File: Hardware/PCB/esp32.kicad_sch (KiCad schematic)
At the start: 6 parts, among them U1 ESP32-S3-WROOM-1

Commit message: added a lot of stuff, going to work on LCD + Touch next
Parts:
- removed R2, R3: 10k, Resistor_SMD:R_0603_1608Metric_Pad0.98x0.95mm_HandSolder, symbol Device:R_Small
- removed U1: ESP32-S3-WROOM-1, RF_Module:ESP32-S3-WROOM-1, symbol RF_Module:ESP32-S3-WROOM-1
- added C14: 1uF, Capacitor_SMD:C_0805_2012Metric_Pad1.18x1.45mm_HandSolder, symbol Device:C_Small
- added C15: 0.1uF, Capacitor_SMD:C_0603_1608Metric_Pad1.08x0.95mm_HandSolder, symbol Device:C_Small
- added D1: BAT60AE6327HTSA1, Diode_SMD:D_SOD-323_HandSoldering, symbol Device:D_Schottky
- added IC3: ESP32-WROVER-E-N8R8, Custom Footprints:ESP32WROVEREN8R8, symbol Custom Symbols:ESP32-WROVER-E-N8R8
- added J3: Programmer, Vendor_Footprints:61200621621, symbol Connector_Generic:Conn_02x03_Odd_Even
- added R2, R6: 10k, Resistor_SMD:R_0603_1608Metric_Pad0.98x0.95mm_HandSolder, symbol Device:R_US
- added SW1: ~, Vendor_Footprints:PTS647SN50SMTR2LFS, symbol Vendor_Symbols:PTS647SN50SMTR2_LFS
- C10: value 0.1u -> 10uF; footprint Capacitor_SMD:C_0603_1608Metric_Pad1.08x0.95mm_HandSolder -> Capacitor_SMD:C_0805_2012Metric; DigiKey Link (none) -> https://www.digikey.com/en/products/detail/samsung-electro-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; MPN (none) -> GRM21BR61H106KE43L; Manufacturer (none) -> Murata Electronics
- C11: value 22u -> 0.1uF; footprint Capacitor_SMD:C_0603_1608Metric_Pad1.08x0.95mm_HandSolder -> Capacitor_SMD:C_0805_2012Metric_Pad1.18x1.45mm_HandSolder; DigiKey Link (none) -> https://www.digikey.com/en/products/detail/samsung-electro-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; MPN (none) -> CL21B104KBCNFNC; Manufacturer (none) -> Samsung Electro-Mechanics
- C9: value 1u -> 10uF; footprint Capacitor_SMD:C_0603_1608Metric_Pad1.08x0.95mm_HandSolder -> Capacitor_SMD:C_0805_2012Metric; DigiKey Link (none) -> https://www.digikey.com/en/products/detail/samsung-electro-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; MPN (none) -> GRM21BR61H106KE43L; Manufacturer (none) -> Murata Electronics
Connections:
- net +3.3V: now also C10.1, C11.1, C9.1, IC3.2 (3V3), R6.1; no longer C10.2, C11.2
- net GND: now also C10.2, C11.2, C9.2, C14.2, IC3.1 (GND_1), IC3.15 (GND_2), IC3.38 (GND_3), IC3.39 (GND_4), IC3.40 (GND_5), IC3.41 (GND_6), IC3.42 (GND_7), IC3.43 (GND_8), IC3.44 (GND_9), IC3.45 (GND_10), IC3.46 (GND_11), IC3.47 (GND_12), J3.4 (Pin_4), R2.2, SW1.3; no longer C10.1, C11.1, C9.1
- new net: D1.2 (A), J3.2 (Pin_2)
- new net: C15.1, SW1.2
- new net: C15.2, SW1.4
- new net +5V: D1.1 (K)
- new net D12: IC3.14 (IO12), R2.1
- new net D13: IC3.16 (IO13)
- new net D14: IC3.13 (IO14)
- new net D15: IC3.23 (IO15)
- new net D18: IC3.30 (IO18)
- new net D19: IC3.31 (IO19)
- new net D2: IC3.24 (IO2)
- new net D21: IC3.33 (IO21)
- new net D22: IC3.36 (IO22)
- new net D23: IC3.37 (IO23)
- new net D25: IC3.10 (IO25)
- new net D26: IC3.11 (IO26)
- new net D27: IC3.12 (IO27)
- new net D32: IC3.8 (IO32)
- new net D33: IC3.9 (IO33)
- new net D34: IC3.6 (IO34)
- new net D35: IC3.7 (IO35)
- new net D36: IC3.4 (SENSOR_VP)
- new net D39: IC3.5 (SENSOR_VN)
- new net D4: IC3.26 (IO4)
- new net D5: IC3.29 (IO5)
- new net ESP-EN: C14.1, IC3.3 (EN), J3.1 (Pin_1), R6.2, SW1.1
- new net ESP-IO0: IC3.25 (IO0), J3.6 (Pin_6)
- new net ESP-RX: IC3.34 (RXD0), J3.5 (Pin_5)
- new net ESP-TX: IC3.35 (TXD0), J3.3 (Pin_3)
- no-connect marks 3 -> 9
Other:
- note added: "Espressif says that IO12 should be kept low when the module is powered on."
- note added: "For recommended soft-start"
- note added: "Recommended decoupling caps"

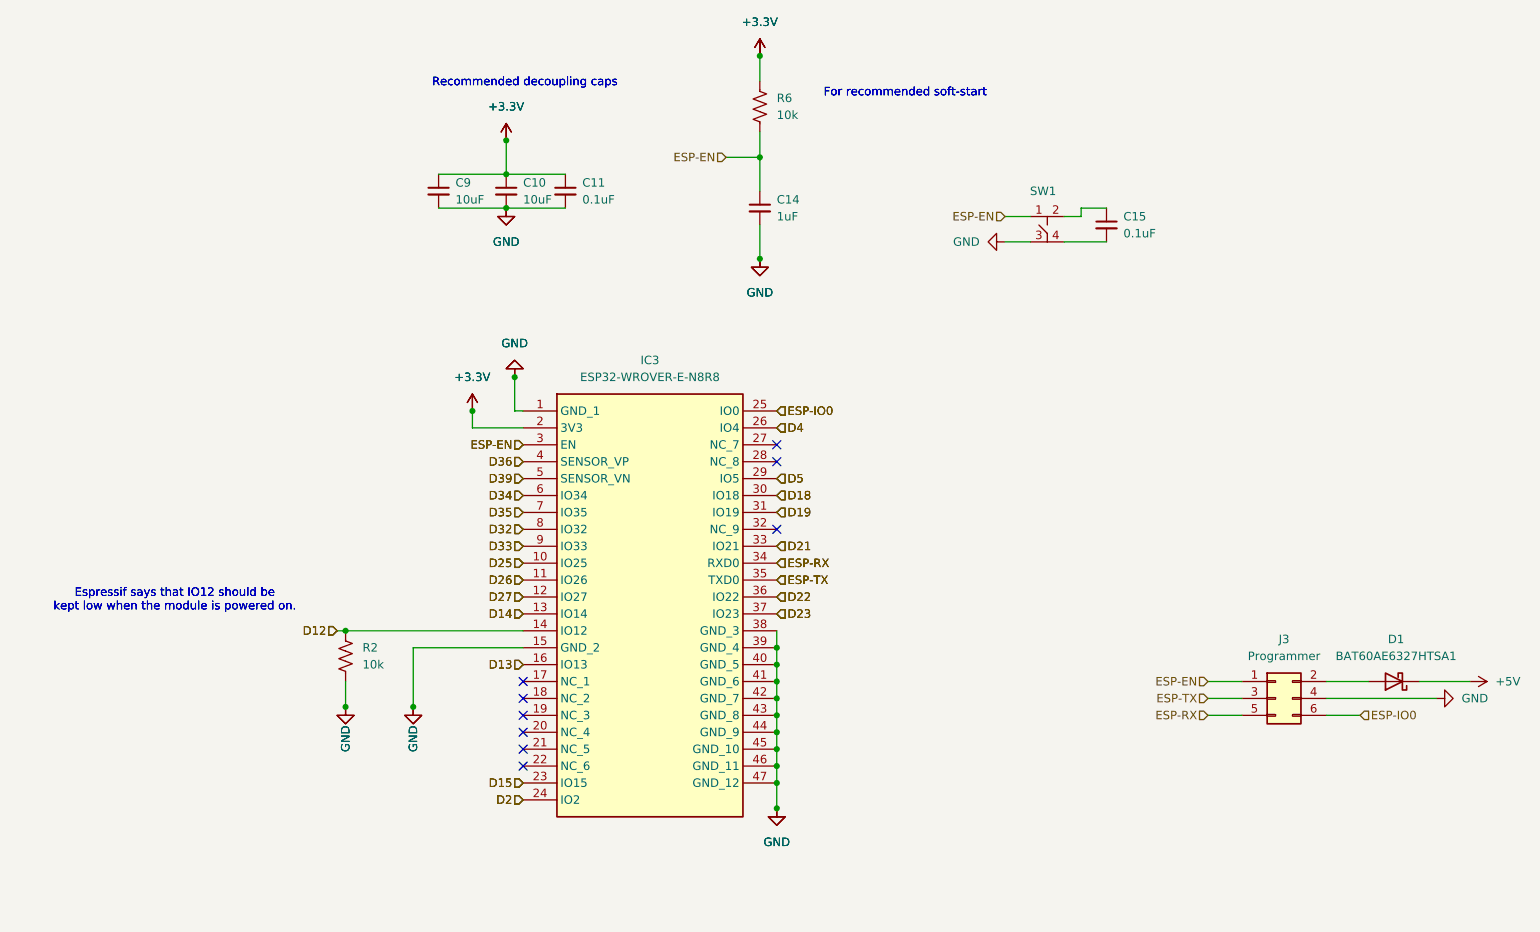
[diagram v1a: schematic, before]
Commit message: switched to making buck converter to save costs and space, and to allow for LDO after 5.5V for better stability
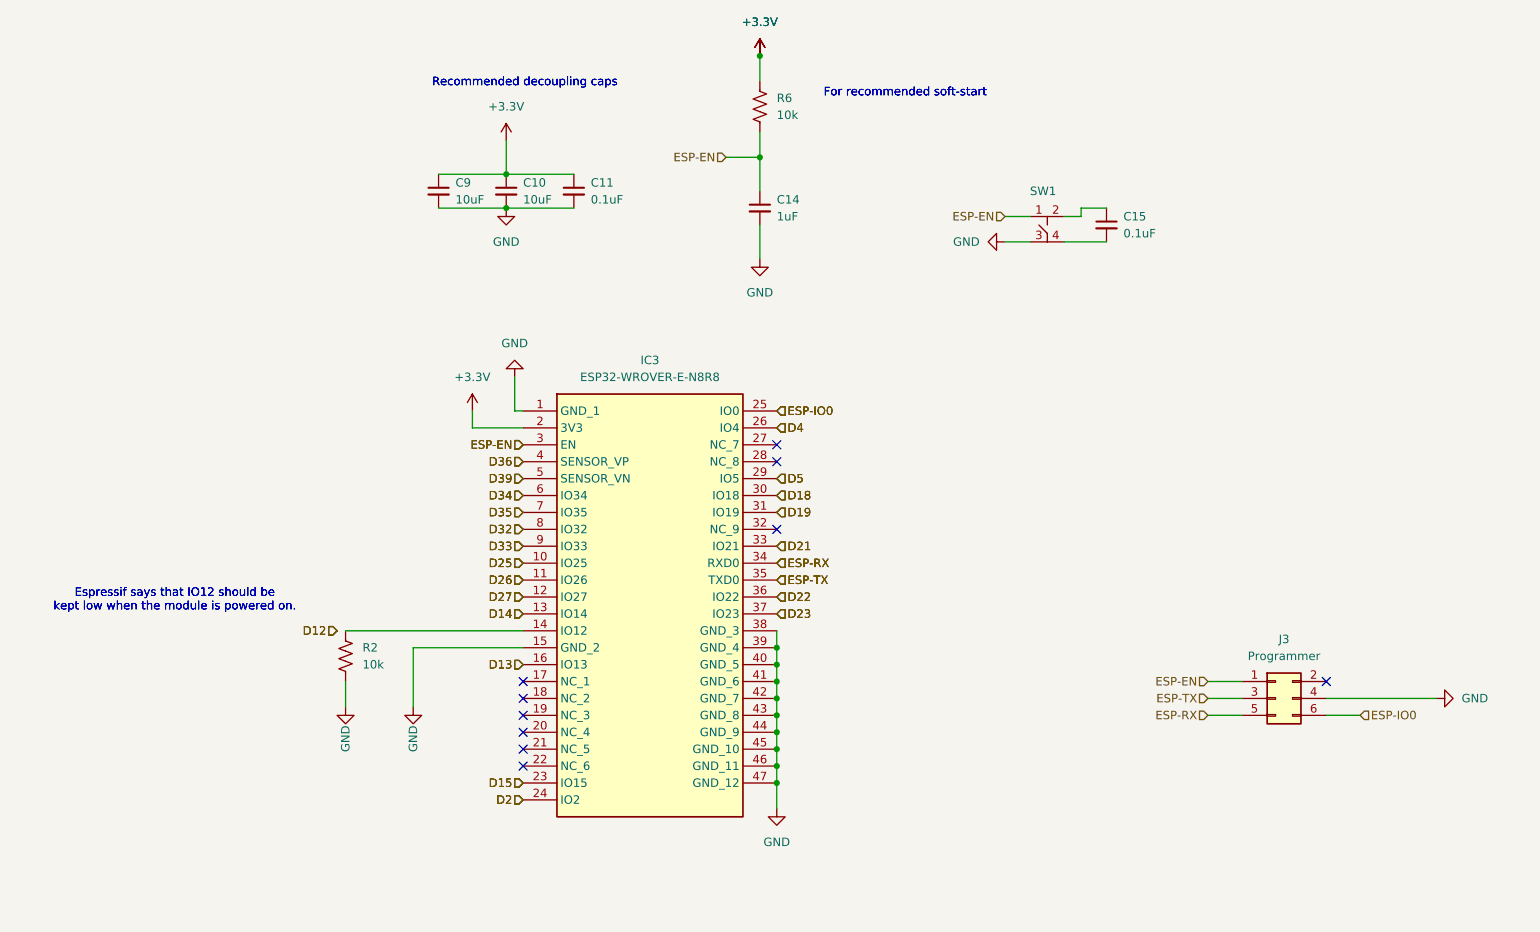
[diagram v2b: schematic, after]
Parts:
- removed D1: BAT60AE6327HTSA1, Diode_SMD:D_SOD-323_HandSoldering, symbol Device:D_Schottky
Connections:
- net D12: no longer IC3.14 (IO12), R2.1
- new net: IC3.14 (IO12), R2.1
- no-connect marks 9 -> 10
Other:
- moved on the sheet: C11

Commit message: consolidated IO for LCD block, broke out hierarchial pins, need to start wiring everything up and then on to layout
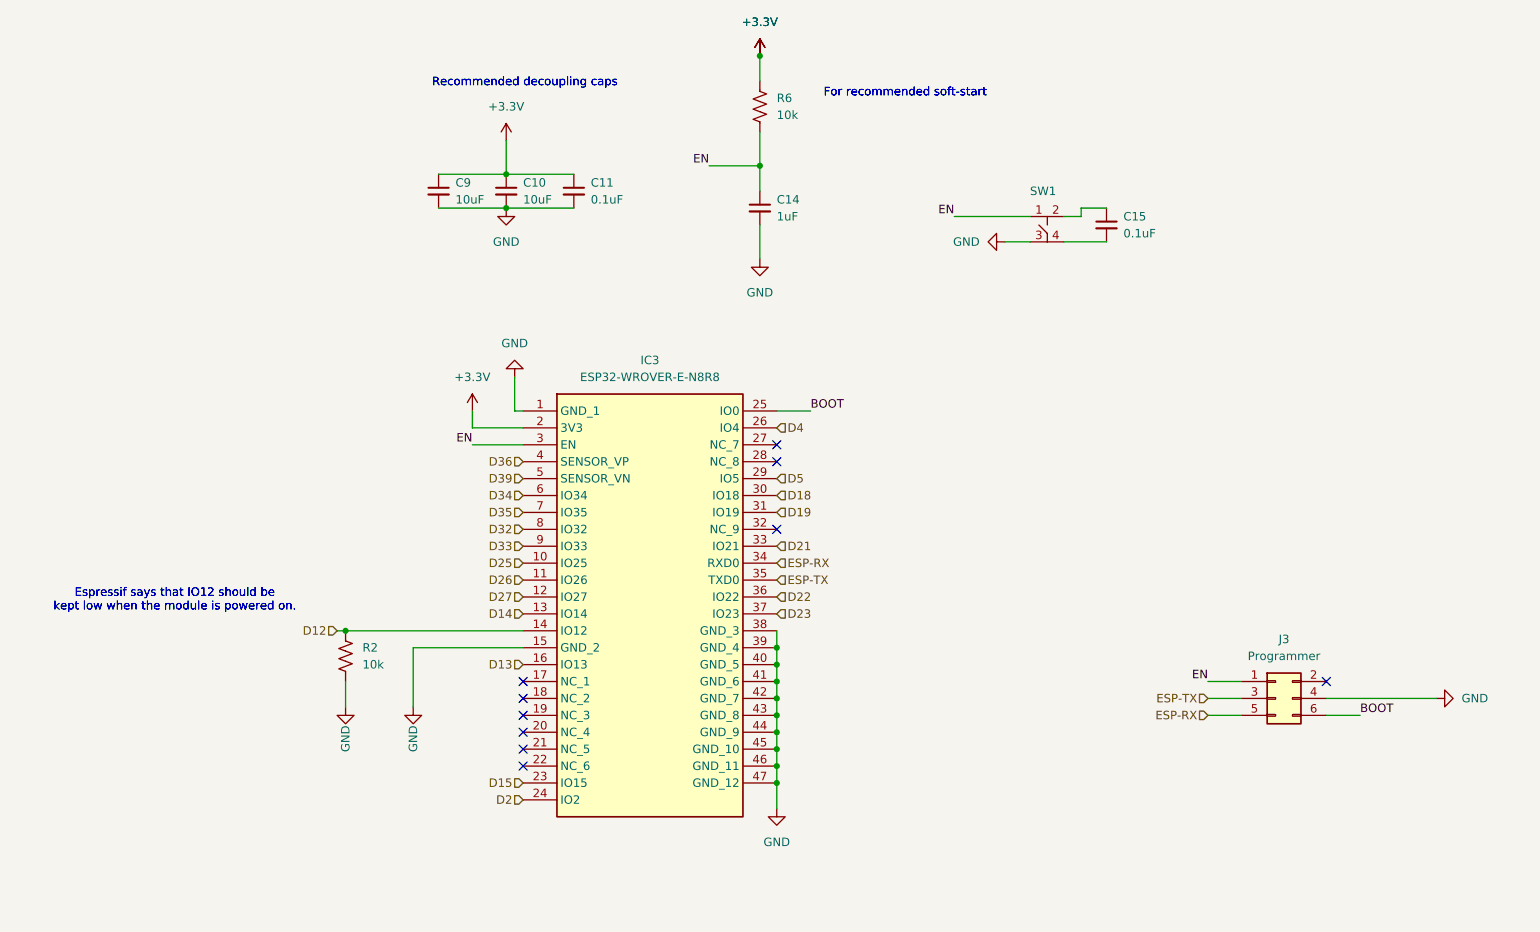
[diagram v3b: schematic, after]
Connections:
- net D12: now also IC3.14 (IO12), R2.1
- net ESP-EN renamed EN
- net ESP-IO0 renamed BOOT

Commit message: overall design is pretty much done, starting layout and routing now
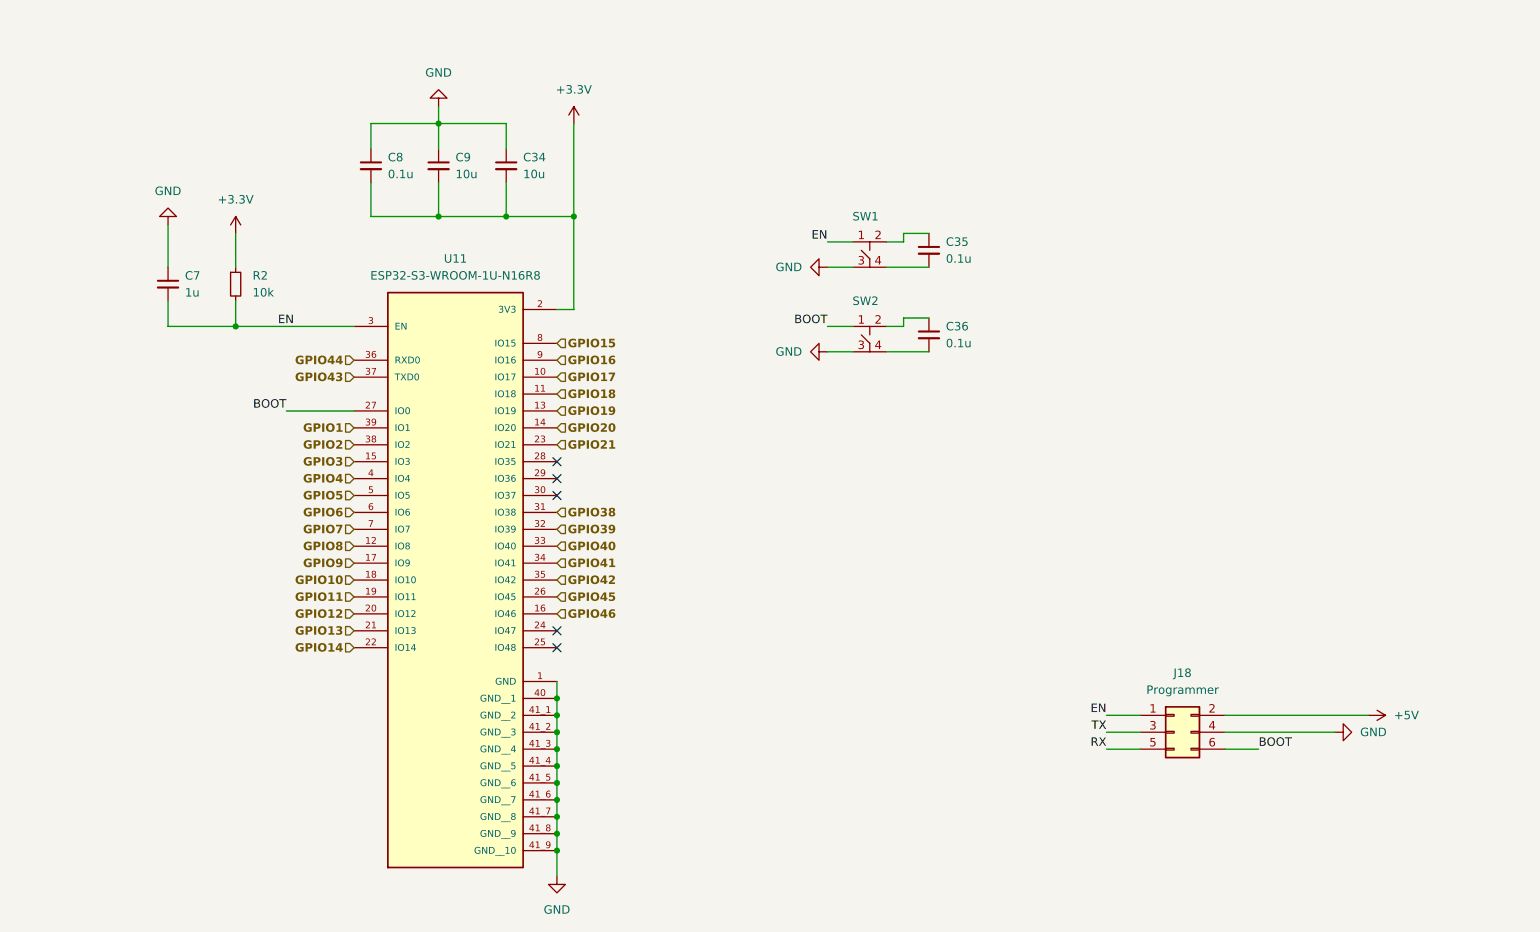
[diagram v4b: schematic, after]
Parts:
- removed C10: 10uF, Capacitor_SMD:C_0805_2012Metric, symbol Device:C_Small
- removed C11: 0.1uF, Capacitor_SMD:C_0805_2012Metric_Pad1.18x1.45mm_HandSolder, symbol Device:C_Small
- removed C14: 1uF, Capacitor_SMD:C_0805_2012Metric_Pad1.18x1.45mm_HandSolder, symbol Device:C_Small
- removed C15: 0.1uF, Capacitor_SMD:C_0603_1608Metric_Pad1.08x0.95mm_HandSolder, symbol Device:C_Small
- removed IC3: ESP32-WROVER-E-N8R8, Custom Footprints:ESP32WROVEREN8R8, symbol Custom Symbols:ESP32-WROVER-E-N8R8
- removed J3: Programmer, Vendor_Footprints:61200621621, symbol Connector_Generic:Conn_02x03_Odd_Even
- removed R2, R6: 10k, Resistor_SMD:R_0603_1608Metric_Pad0.98x0.95mm_HandSolder, symbol Device:R_US
- added C34: 10u, Capacitor_SMD:C_0805_2012Metric_Pad1.18x1.45mm_HandSolder, symbol Device:C_Small
- added C35, C36, C8: 0.1u, Capacitor_SMD:C_0603_1608Metric_Pad1.08x0.95mm_HandSolder, symbol Device:C_Small
- added C7: 1u, Capacitor_SMD:C_0603_1608Metric_Pad1.08x0.95mm_HandSolder, symbol Device:C_Small
- added J18: Programmer, Vendor_Footprints:61200621621, symbol Connector_Generic:Conn_02x03_Odd_Even
- added R2: 10k, Resistor_SMD:R_0603_1608Metric_Pad0.98x0.95mm_HandSolder, symbol Device:R_Small
- added SW2: ~, Vendor_Footprints:PTS647SN50SMTR2LFS, symbol Vendor_Symbols:PTS647SN50SMTR2_LFS
- added U11: ESP32-S3-WROOM-1U-N16R8, Vendor_Footprints:XCVR_ESP32-S3-WROOM-1U-N16R8, symbol Vendor_Symbols:ESP32-S3-WROOM-1U-N16R8
- C9: value 10uF -> 10u; footprint Capacitor_SMD:C_0805_2012Metric -> Capacitor_SMD:C_0805_2012Metric_Pad1.18x1.45mm_HandSolder; DigiKey Link https://www.digikey.com/en/products/detail/samsung-electro-mechanics/CL21A106KOQNNNE/3886754 -> https://www.digikey.com/en/products/detail/samsung-electro-mechanics/CL21A106KOQNNNG/3894417; MPN GRM21BR61H106KE43L -> CL21A106KOQNNNG; Manufacturer Murata Electronics -> Samsung Electro-Mechanics
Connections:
- net +3.3V: now also C9.2, C34.2, C8.2, R2.1, U11.2 (3V3); no longer C9.1
- net BOOT: now also J18.6 (Pin_6), SW2.1, U11.27 (IO0)
- net EN: now also C7.2, J18.1 (Pin_1), R2.2, U11.3 (EN)
- net GND: now also C9.1, C34.1, C7.1, C8.1, J18.4 (Pin_4), SW2.3, U11.1 (GND), U11.40 (GND__1), U11.41_1 (GND__2), U11.41_2 (GND__3), U11.41_3 (GND__4), U11.41_4 (GND__5), U11.41_5 (GND__6), U11.41_6 (GND__7), U11.41_7 (GND__8), U11.41_8 (GND__9), U11.41_9 (GND__10); no longer C9.2
- net at SW1.2: now also C35.1
- net at SW1.4: now also C35.2
- new net: C36.1, SW2.2
- new net: C36.2, SW2.4
- new net +5V: J18.2 (Pin_2)
- new net GPIO1: U11.39 (IO1)
- new net GPIO10: U11.18 (IO10)
- new net GPIO11: U11.19 (IO11)
- new net GPIO12: U11.20 (IO12)
- new net GPIO13: U11.21 (IO13)
- new net GPIO14: U11.22 (IO14)
- new net GPIO15: U11.8 (IO15)
- new net GPIO16: U11.9 (IO16)
- new net GPIO17: U11.10 (IO17)
- new net GPIO18: U11.11 (IO18)
- new net GPIO19: U11.13 (IO19)
- new net GPIO2: U11.38 (IO2)
- new net GPIO20: U11.14 (IO20)
- new net GPIO21: U11.23 (IO21)
- new net GPIO3: U11.15 (IO3)
- new net GPIO38: U11.31 (IO38)
- new net GPIO39: U11.32 (IO39)
- new net GPIO4: U11.4 (IO4)
- new net GPIO40: U11.33 (IO40)
- new net GPIO41: U11.34 (IO41)
- new net GPIO42: U11.35 (IO42)
- new net GPIO43: U11.37 (TXD0)
- new net GPIO44: U11.36 (RXD0)
- new net GPIO45: U11.26 (IO45)
- new net GPIO46: U11.16 (IO46)
- new net GPIO5: U11.5 (IO5)
- new net GPIO6: U11.6 (IO6)
- new net GPIO7: U11.7 (IO7)
- new net GPIO8: U11.12 (IO8)
- new net GPIO9: U11.17 (IO9)
- new net RX: J18.5 (Pin_5)
- new net TX: J18.3 (Pin_3)
- no-connect marks 10 -> 5
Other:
- note removed: "Espressif says that IO12 should be kept low when the module is powered on."
- note removed: "For recommended soft-start"
- note removed: "Recommended decoupling caps"

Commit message: pcb layout and routing pretty much done, checking DRC
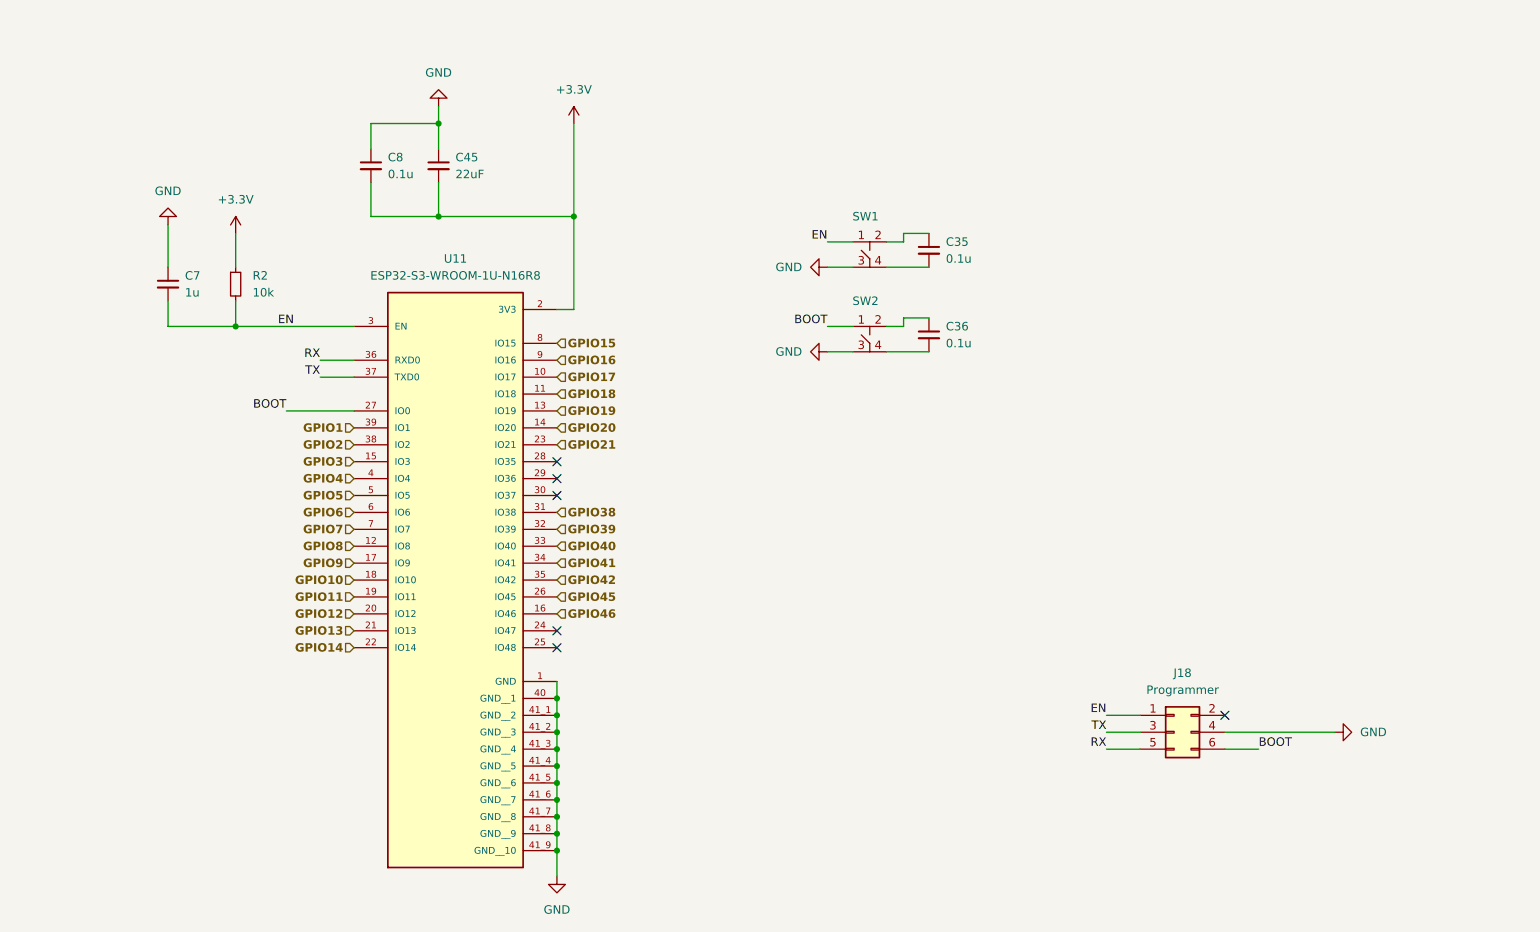
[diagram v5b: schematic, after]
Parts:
- removed C34, C9: 10u, Capacitor_SMD:C_0805_2012Metric_Pad1.18x1.45mm_HandSolder, symbol Device:C_Small
- added C45: 22uF, Capacitor_SMD:C_0805_2012Metric_Pad1.18x1.45mm_HandSolder, symbol Device:C_Small
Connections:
- net GPIO43 is gone; now on net TX: U11.37 (TXD0)
- net GPIO44 is gone; now on net RX: U11.36 (RXD0)
- net +3.3V: now also C45.2
- net GND: now also C45.1
- net +5V: no longer names the net of J18.2 (Pin_2)
- no-connect marks 5 -> 6
